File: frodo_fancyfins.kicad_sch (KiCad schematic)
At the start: 31 parts, among them J1 Molex MicroFit 2x3, J2 Molex MicroFit 2x3, J4 SWD Header, U1 STM32F072RBTx, U2 MCP2562-E-SN, U3 AZ1117-3.3, Y1 8MHz 12pF

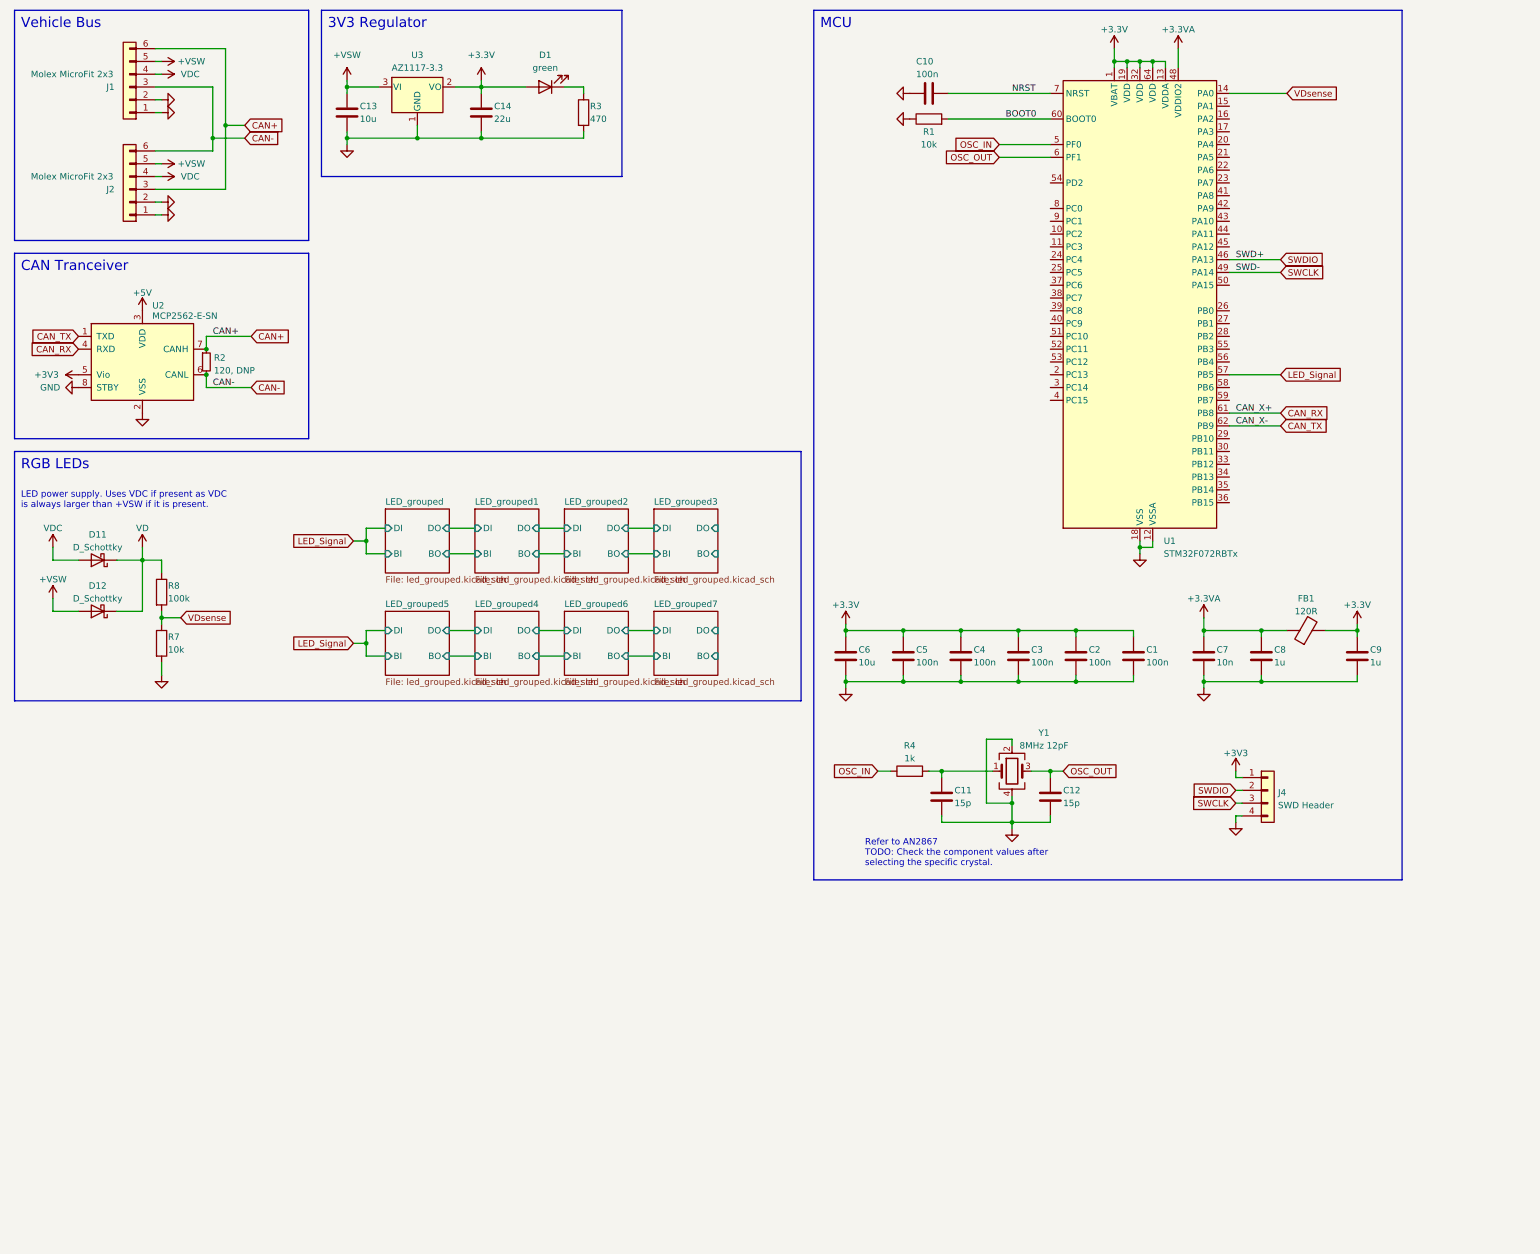
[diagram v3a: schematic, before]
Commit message: Add RF module to Schematics
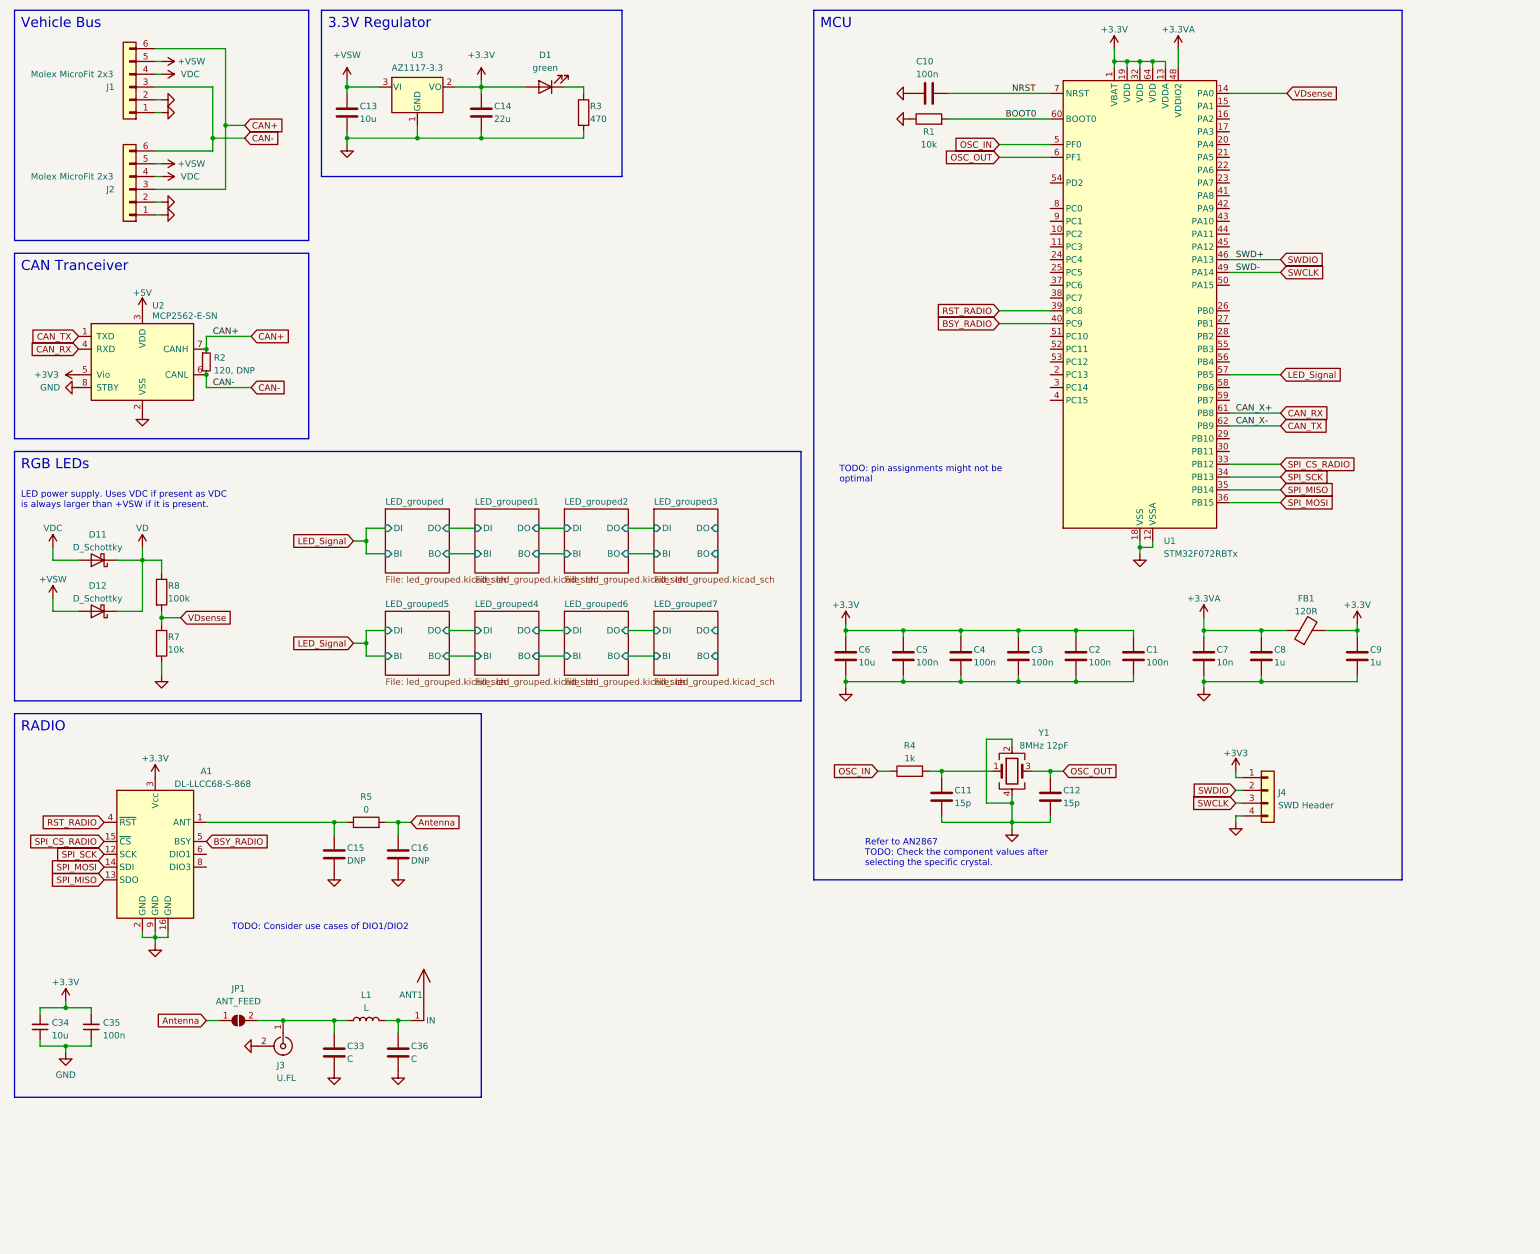
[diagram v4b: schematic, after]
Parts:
- added A1: DL-LLCC68-S-868, frodo_fancyfins:DL-LLCC68-S-868, symbol frodo_fancyfins:DL-LLCC68-S-868
- added ANT1: ~, frodo_fancyfins:meandering_monopole_antenna_868MHz, symbol frodo_fancyfins:meandering_monopole_antenna_868MHz
- added C15, C16: DNP, symbol Device:C
- added C33, C36: C, symbol Device:C
- added C34: 10u, Capacitor_SMD:C_1206_3216Metric, symbol Device:C_Small
- added C35: 100n, Capacitor_SMD:C_0603_1608Metric, symbol Device:C_Small
- added J3: U.FL, symbol Connector:Conn_Coaxial
- added JP1: ANT_FEED, symbol Jumper:SolderJumper_2_Open
- added L1: L, symbol Device:L
- added R5: 0, symbol Device:R
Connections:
- net +3.3V: now also A1.3 (Vcc), C34.2, C35.2
- net GND: now also A1.16 (GND), A1.2 (GND), A1.9 (GND), C15.2, C16.2, C33.2, C34.1, C35.1, C36.2, J3.2 (Ext)
- net SPI_CS_RADIO: now reaches U1.33 (PB12)
- net SPI_CS_RADIO: now also A1.15 (~{CS})
- net SPI_SCK: now reaches U1.34 (PB13)
- net SPI_SCK: now also A1.12 (SCK)
- net SPI_MISO: now reaches U1.35 (PB14)
- net SPI_MISO: now also A1.13 (SDO)
- net SPI_MOSI: now reaches U1.36 (PB15)
- net SPI_MOSI: now also A1.14 (SDI)
- net RST_RADIO: now reaches U1.39 (PC8)
- net RST_RADIO: now also A1.4 (~{RST})
- net BSY_RADIO: now reaches U1.40 (PC9)
- net BSY_RADIO: now also A1.5 (BSY)
- new net: C33.1, J3.1 (In), JP1.2 (B), L1.1
- new net: A1.1 (ANT), C15.1, R5.1
- new net: ANT1.1 (IN), C36.1, L1.2
- new net Antenna: C16.1, JP1.1 (A), R5.2
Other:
- note added: "3.3V Regulator"
- note added: "RADIO"
- note added: "TODO: Consider use cases of DIO1/DIO2"
- note added: "TODO: pin assignments might not be optimal"
- note removed: "3V3 Regulator"

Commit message: Add strain gauge schematics
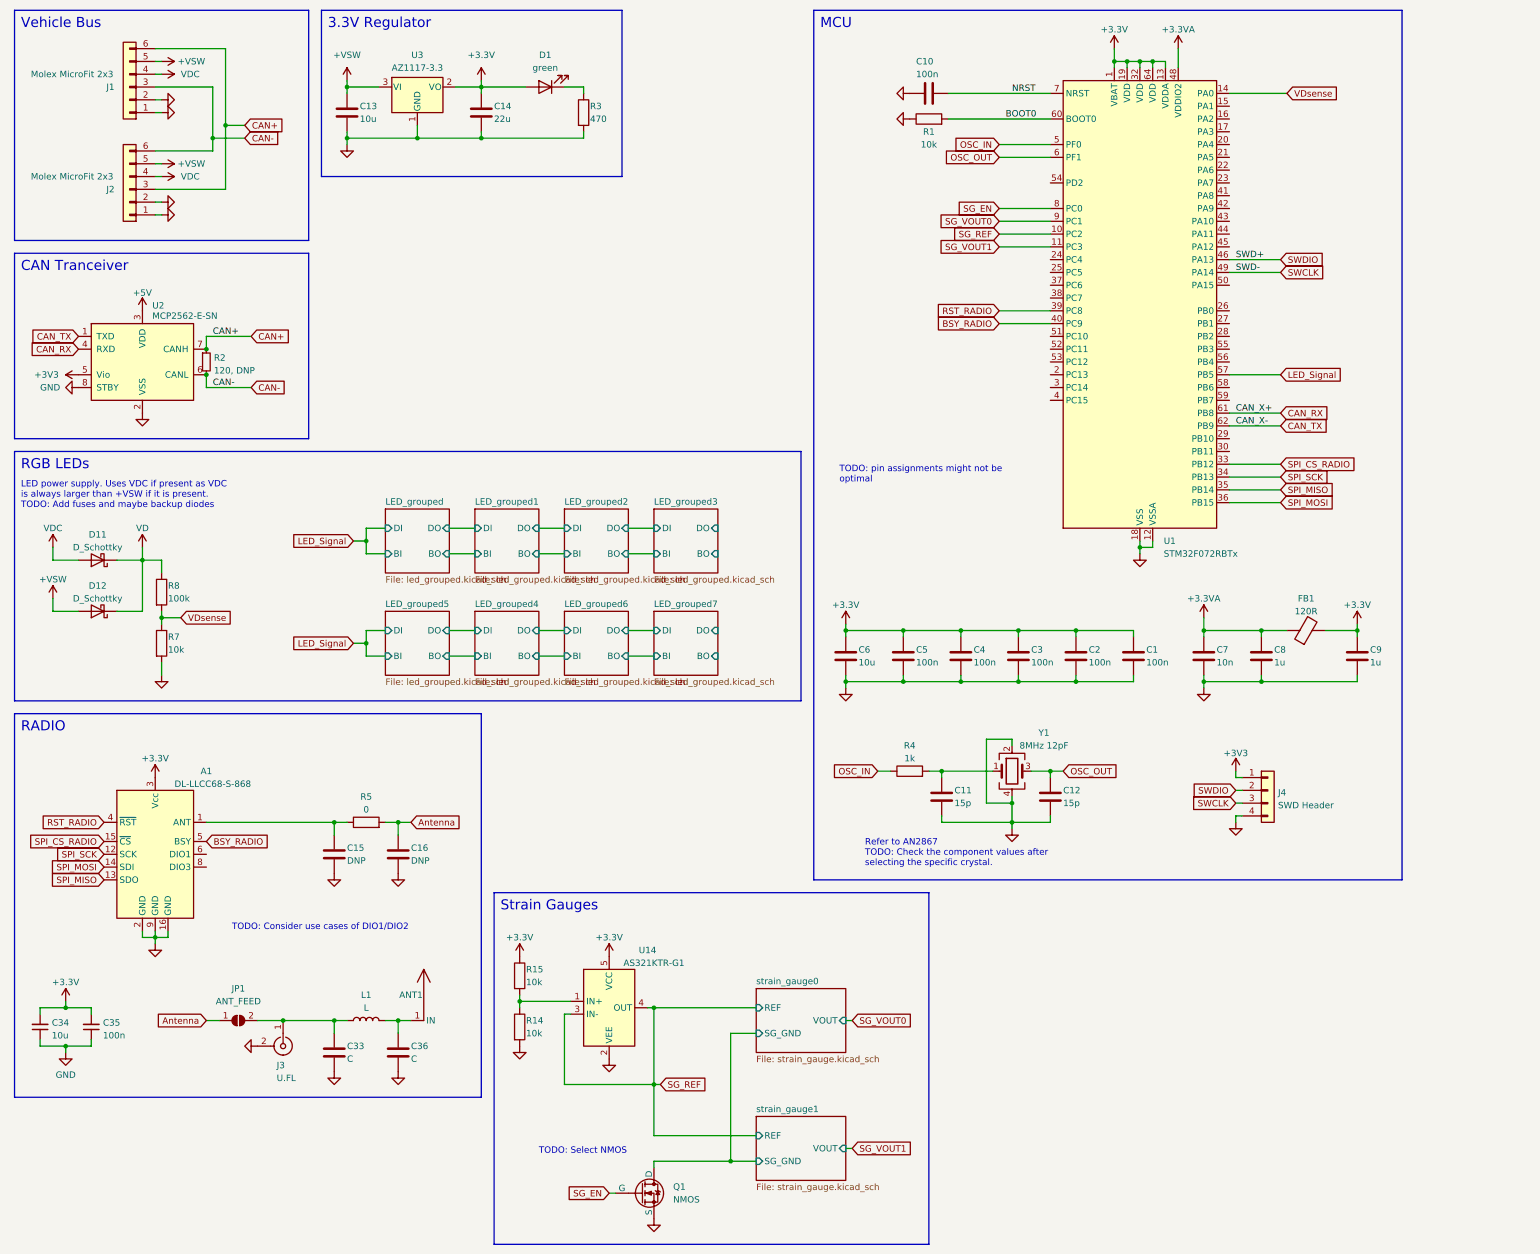
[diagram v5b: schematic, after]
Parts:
- added Q1: NMOS, symbol Simulation_SPICE:NMOS
- added R14, R15: 10k, symbol Device:R
- added U14: AS321KTR-G1, symbol frodo_fancyfins:AS321KTR-G1
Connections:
- net +3.3V: now also R15.1, U14.5 (VCC)
- net GND: now also Q1.3 (S), R14.2, U14.2 (VEE)
- net SG_REF: now reaches U1.10 (PC2)
- net SG_REF: now also U14.3 (IN-), U14.4 (OUT)
- net SG_VOUT1: now reaches U1.11 (PC3)
- net SG_EN: now reaches U1.8 (PC0)
- net SG_EN: now also Q1.2 (G)
- net SG_VOUT0: now reaches U1.9 (PC1)
- new net: R14.1, R15.2, U14.1 (IN+)
- new net strain_gauge0/SG_GND: Q1.1 (D)
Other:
- added sheet strain_gauge0 (strain_gauge.kicad_sch)
- added sheet strain_gauge1 (strain_gauge.kicad_sch)
- note added: "LED power supply. Uses VDC if present as VDC is always larger than +VSW if it is present. TODO: Add fuses and maybe backup diodes"
- note added: "Strain Gauges"
- note added: "TODO: Select NMOS"
- note removed: "LED power supply. Uses VDC if present as VDC is always larger than +VSW if it is present."

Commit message: 3.3V and 5V power supply tweaks
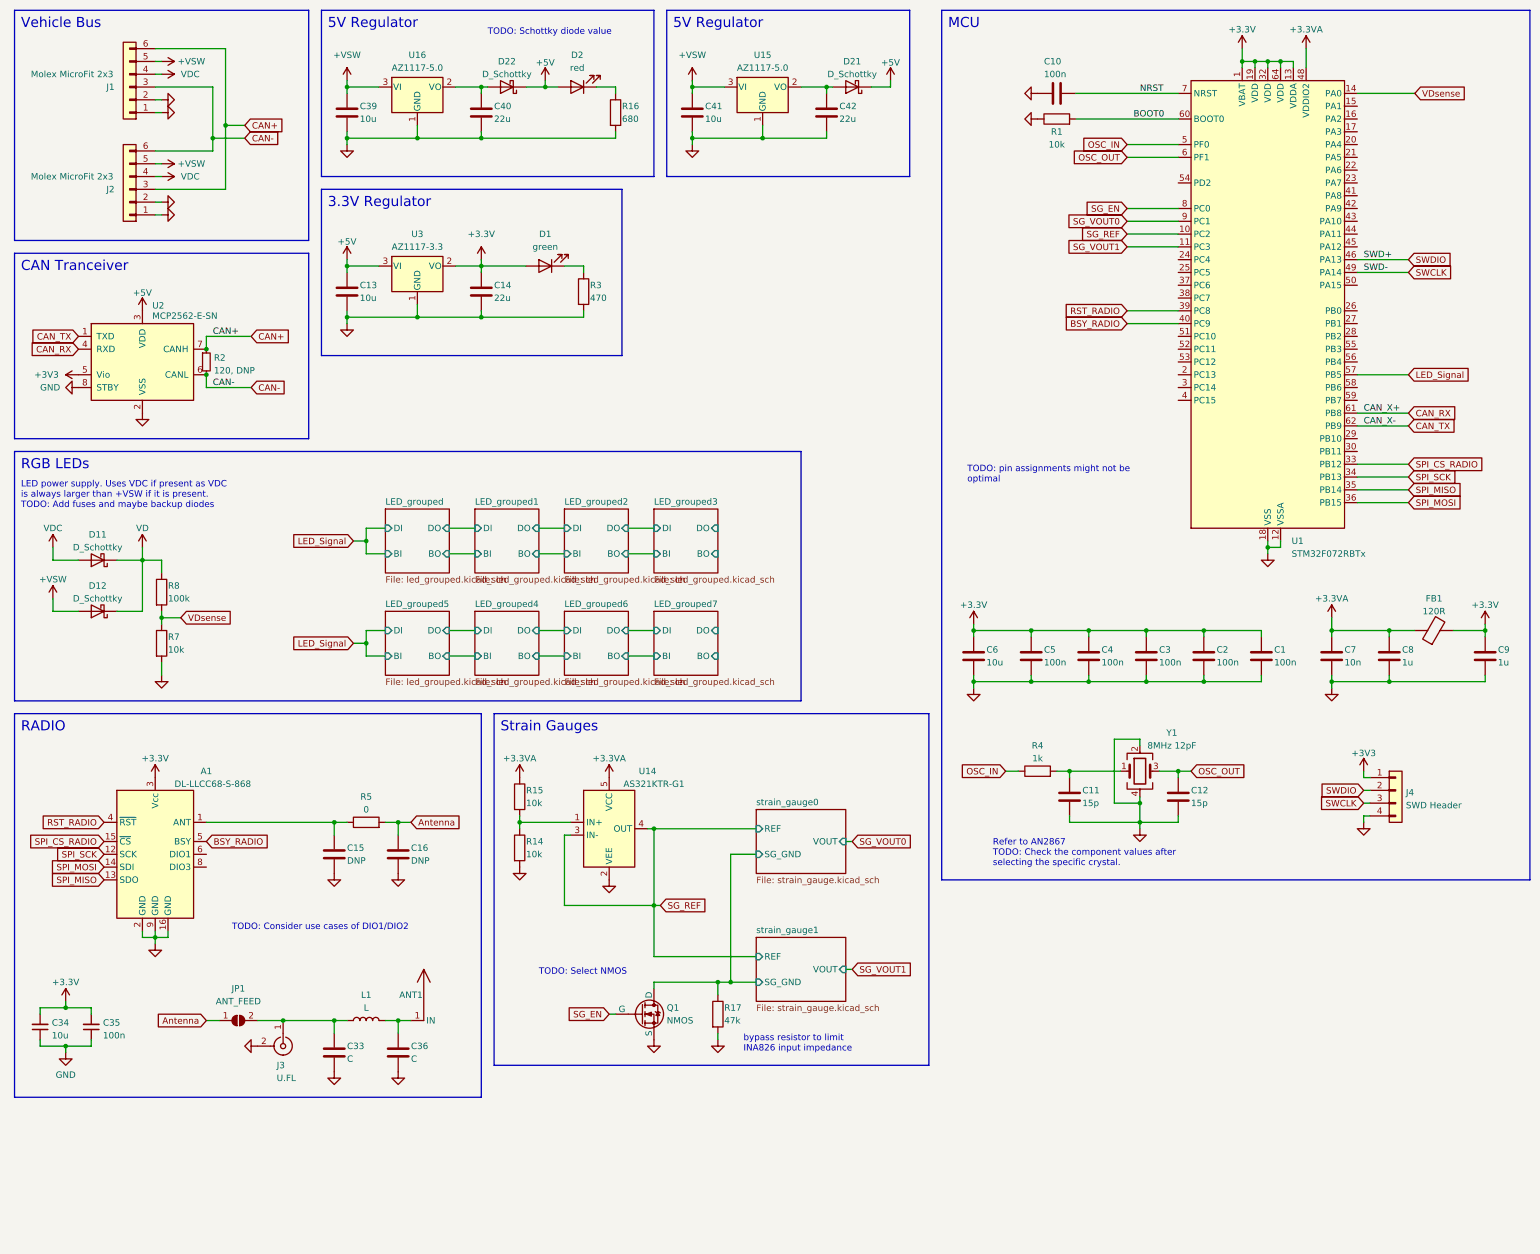
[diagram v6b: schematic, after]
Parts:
- added C39, C41: 10u, symbol Device:C
- added C40, C42: 22u, symbol Device:C
- added D2: red, symbol Device:LED
- added D21, D22: D_Schottky, symbol Device:D_Schottky
- added R16: 680, symbol Device:R
- added R17: 47k, symbol Device:R
- added U15, U16: AZ1117-5.0, symbol Regulator_Linear:AZ1117-5.0
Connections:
- net +3.3V: no longer R15.1, U14.5 (VCC)
- net +3.3VA: now also R15.1, U14.5 (VCC)
- net +5V: now also C13.1, U3.3 (VI), D2.2 (A), D21.1 (K), D22.1 (K)
- net +VSW: now also C39.1, C41.1, U15.3 (VI), U16.3 (VI); no longer C13.1, U3.3 (VI)
- net GND: now also C39.2, C40.2, C41.2, C42.2, R16.2, R17.2, U15.1 (GND), U16.1 (GND)
- net strain_gauge0/SG_GND: now also R17.1
- new net: C40.1, D22.2 (A), U16.2 (VO)
- new net: C42.1, D21.2 (A), U15.2 (VO)
- new net: D2.1 (K), R16.1
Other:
- note added: "5V Regulator"
- note added: "TODO: Schottky diode value"
- note added: "bypass resistor to limit INA826 input impedance"
- moved on the sheet: C1, C10, C11, C12, C13, C14, C2, C3, C4, C5, C6, C7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
